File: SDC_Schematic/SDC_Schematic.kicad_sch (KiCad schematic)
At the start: 23 parts, among them J1 Screw_Terminal_01x02, J2 Screw_Terminal_01x02, J3 Screw_Terminal_01x02, J4 Conn_01x04, J5 Conn_01x04, J6 Conn_01x06_Socket, J7 Conn_01x03_Pin, J8 Conn_01x04, SW1 SW_SPST, U1 ATmega8A-P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

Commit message: modified schematic
added SPI port, capacitors for the servo & uC and barrel jack for power input
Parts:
- removed J3: Screw_Terminal_01x02, Capacitor_THT:C_Disc_D3.0mm_W1.6mm_P2.50mm, symbol Connector:Screw_Terminal_01x02
- added C5: 100nF, Capacitor_THT:C_Disc_D5.0mm_W2.5mm_P2.50mm, symbol Device:C_Small
- added C6: 100uF, symbol Device:C_Polarized
- added C7: 220uF, symbol Device:C_Polarized
- added J10: Jack-DC, symbol Connector:Jack-DC
- added J9: Conn_01x06_Socket, Connector_PinSocket_2.54mm:PinSocket_1x06_P2.54mm_Horizontal, symbol Connector:Conn_01x06_Socket
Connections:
- net +5V: now also C5.2, C6.1, C7.1, J9.6 (Pin_6)
- net GND: now also C5.1, C6.2, C7.2, J9.1 (Pin_1)
- net at U4.1 (IN+): now also J10.1
- net at U4.2 (IN-): now also J10.2
- net RST: now reaches C3.2, R1.2, SW1.2 (B), U1.1 (PC6/~{RESET})
- net RST: now also J9.5 (Pin_5)
- net MISO: now reaches U1.18 (PB4)
- net MISO: now also J9.3 (Pin_3)
- net SCK: now reaches U1.19 (PB5)
- net SCK: now also J9.4 (Pin_4)
- net SERVO renamed SERVO/MOSI
- net SERVO/MOSI: now also J9.2 (Pin_2)
- no-connect marks 8 -> 6
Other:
- note added: "SPI-For-Programming"
- moved on the sheet: J4, J5, J6, J7, J8, R2, R3, R4, R5, R6

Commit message: added part list
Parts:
- C6, C7: footprint (none) -> Capacitor_THT:CP_Radial_D6.3mm_P2.50mm
- J10: footprint (none) -> Connector_BarrelJack:BarrelJack_Horizontal
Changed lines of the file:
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@@
       (effects (font (size 1.27 1.27)) (justify left))
     )
-    (property "Footprint" "" (at 206.7052 45.72 0)
+    (property "Footprint" "Capacitor_THT:CP_Radial_D6.3mm_P2.50mm" (at 206.7052 45.72 0)
       (effects (font (size 1.27 1.27)) hide)
     )
@@
       (effects (font (size 1.27 1.27)))
     )
-    (property "Footprint" "" (at 40.64 45.466 0)
+    (property "Footprint" "Connector_BarrelJack:BarrelJack_Horizontal" (at 40.64 45.466 0)
       (effects (font (size 1.27 1.27)) hide)
     )
@@
       (effects (font (size 1.27 1.27)) (justify left))
     )
-    (property "Footprint" "" (at 157.1752 64.77 0)
-      (effects (font (size 1.27 1.27)) hide)
-    )
+    (property "Footprint" "Capacitor_THT:CP_Radial_D6.3mm_P2.50mm" (at 157.1752 64.77 0)
+      (effects (font (size 1.27 1.27)) hide)
+    )

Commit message: added mounting hole
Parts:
- added H1, H2, H3, H4: MountingHole, MountingHole:MountingHole_3.5mm, symbol Mechanical:MountingHole
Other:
- note added: "ANODE"
- note added: "CATHODE"
- note added: "EMITTER"
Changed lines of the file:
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@@
+    (stroke (width 0) (type default))
+  )
+  (polyline (pts (xy 125.73 179.07) (xy 125.73 160.02))
     (stroke (width 0) (type default))
   )
@@
     (stroke (width 0) (type default))
   )
+  (polyline (pts (xy 82.55 160.02) (xy 125.73 160.02))
+    (stroke (width 0) (type default))
+  )
   (polyline (pts (xy 29.21 58.42) (xy 95.25 58.42))
     (stroke (width 0) (type default))
@@
     (stroke (width 0) (type default))
   )
+  (polyline (pts (xy 82.55 179.07) (xy 125.73 179.07))
+    (stroke (width 0) (type default))
+  )
   (wire (pts (xy 139.7 147.32) (xy 140.97 147.32))
     (stroke (width 0) (type default))
@@
   )
   (wire (pts (xy 208.28 88.9) (xy 189.23 88.9))
+    (stroke (width 0) (type default))
+  )
+  (polyline (pts (xy 82.55 160.02) (xy 82.55 179.07))
     (stroke (width 0) (type default))
   )
@@
     (effects (font (size 1.5 1.5)) (justify left bottom))
   )
+  (text "EMITTER" (at 50.8 121.92 0)
+    (effects (font (size 1.27 1.27)) (justify left bottom))
+  )
+  (text "ANODE" (at 52.07 116.84 0)
+    (effects (font (size 1.27 1.27)) (justify left bottom))
+  )
   (text "SERVO" (at 199.39 29.21 0)
     (effects (font (size 3 3) (thickness 0.4) bold) (justify left bottom))
   )
+  (text "EMITTER" (at 50.8 144.78 0)
+    (effects (font (size 1.27 1.27)) (justify left bottom))
+  )
+  (text "CATHODE" (at 50.8 119.38 0)
+    (effects (font (size 1.27 1.27)) (justify left bottom))
+  )
+  (text "ANODE" (at 52.07 139.7 0)
+    (effects (font (size 1.27 1.27)) (justify left bottom))
+  )
   (text "POWER SUPPLY" (at 29.21 29.21 0)
     (effects (font (size 3 3) (thickness 0.6) bold) (justify left bottom))
@@
     (effects (font (size 3 3) bold) (justify left bottom))
   )
+  (text "CATHODE" (at 50.8 142.24 0)
+    (effects (font (size 1.27 1.27)) (justify left bottom))
+  )
   (label "RST" (at 48.26 170.18 180) (fields_autoplaced)
     (effects (font (size 1.27 1.27)) (justify right bottom))
@@
     (effects (font (size 1.27 1.27) bold) (justify left bottom))
   )
-  (label "EMITTER" (at 50.8 144.78 0) (fields_autoplaced)
-    (effects (font (size 1.27 1.27)) (justify left bottom))
-  )
   (label "SERVO{slash}MOSI" (at 167.64 88.9 180) (fields_autoplaced)
     (effects (font (size 1.27 1.27)) (justify right bottom))
   )
   (label "EN3,4" (at 201.93 109.22 0) (fields_autoplaced)
-    (effects (font (size 1.27 1.27)) (justify left bottom))
-  )
-  (label "CATHODE" (at 50.8 142.24 0) (fields_autoplaced)
     (effects (font (size 1.27 1.27)) (justify left bottom))
   )
@@
     (effects (font (size 1.27 1.27) bold) (justify left bottom))
   )
-  (label "ANODE" (at 58.42 116.84 180) (fields_autoplaced)
-    (effects (font (size 1.27 1.27)) (justify right bottom))
-  )
   (label "RX0" (at 203.2 154.94 0) (fields_autoplaced)
     (effects (font (size 1.27 1.27)) (justify left bottom))
@@
     (effects (font (size 1.27 1.27)) (justify right bottom))
   )
-  (label "CATHODE" (at 50.8 119.38 0) (fields_autoplaced)
-    (effects (font (size 1.27 1.27)) (justify left bottom))
-  )
-  (label "ANODE" (at 52.07 139.7 0) (fields_autoplaced)
-    (effects (font (size 1.27 1.27)) (justify left bottom))
-  )
   (label "EN1,2" (at 201.93 93.98 0) (fields_autoplaced)
     (effects (font (size 1.27 1.27)) (justify left bottom))
@@
   (label "EN1,2" (at 163.83 83.82 180) (fields_autoplaced)
     (effects (font (size 1.27 1.27)) (justify right bottom))
-  )
-  (label "EMITTER" (at 50.8 121.92 0) (fields_autoplaced)
-    (effects (font (size 1.27 1.27)) (justify left bottom))
   )
   (symbol (lib_id "Connector:Conn_01x06_Socket") (at 36.83 175.26 180) (unit 1)
@@
     )
   )
+  (symbol (lib_id "Mechanical:MountingHole") (at 107.95 163.83 0) (unit 1)
+    (in_bom yes) (on_board yes) (dnp no) (fields_autoplaced)
+    (property "Reference" "H2" (at 110.49 162.56 0)
+      (effects (font (size 1.27 1.27)) (justify left))
+    )
+    (property "Value" "MountingHole" (at 110.49 165.1 0)
+      (effects (font (size 1.27 1.27)) (justify left))
+    )
+    (property "Footprint" "MountingHole:MountingHole_3.5mm" (at 107.95 163.83 0)
+      (effects (font (size 1.27 1.27)) hide)
+    )
+    (property "Datasheet" "~" (at 107.95 163.83 0)
+      (effects (font (size 1.27 1.27)) hide)
+    )
+    (instances
+      (project "SDC_Schematic"
+        (path "/f4146ac7-8f5d-4d47-a7f7-55c436dc7aff"
+          (reference "H2") (unit 1)
+        )
+      )
+    )
+  )
   (symbol (lib_id "Device:R") (at 52.07 147.32 90) (unit 1)
     (in_bom yes) (on_board yes) (dnp no)
@@
     )
   )
+  (symbol (lib_id "Mechanical:MountingHole") (at 107.95 173.99 0) (unit 1)
+    (in_bom yes) (on_board yes) (dnp no) (fields_autoplaced)
+    (property "Reference" "H4" (at 110.49 172.72 0)
+      (effects (font (size 1.27 1.27)) (justify left))
+    )
+    (property "Value" "MountingHole" (at 110.49 175.26 0)
+      (effects (font (size 1.27 1.27)) (justify left))
+    )
+    (property "Footprint" "MountingHole:MountingHole_3.5mm" (at 107.95 173.99 0)
+      (effects (font (size 1.27 1.27)) hide)
+    )
+    (property "Datasheet" "~" (at 107.95 173.99 0)
+      (effects (font (size 1.27 1.27)) hide)
+    )
+    (instances
+      (project "SDC_Schematic"
+        (path "/f4146ac7-8f5d-4d47-a7f7-55c436dc7aff"
+          (reference "H4") (unit 1)
+        )
+      )
+    )
+  )
   (symbol (lib_id "power:GND") (at 140.97 148.59 0) (unit 1)
     (in_bom yes) (on_board yes) (dnp no) (fields_autoplaced)
@@
         (path "/f4146ac7-8f5d-4d47-a7f7-55c436dc7aff"
           (reference "#PWR04") (unit 1)
+        )
+      )
+    )
+  )
+  (symbol (lib_id "Mechanical:MountingHole") (at 86.36 173.99 0) (unit 1)
+    (in_bom yes) (on_board yes) (dnp no) (fields_autoplaced)
+    (property "Reference" "H3" (at 88.9 172.72 0)
+      (effects (font (size 1.27 1.27)) (justify left))
+    )
+    (property "Value" "MountingHole" (at 88.9 175.26 0)
+      (effects (font (size 1.27 1.27)) (justify left))
+    )
+    (property "Footprint" "MountingHole:MountingHole_3.5mm" (at 86.36 173.99 0)
+      (effects (font (size 1.27 1.27)) hide)
+    )
+    (property "Datasheet" "~" (at 86.36 173.99 0)
+      (effects (font (size 1.27 1.27)) hide)
+    )
+    (instances
+      (project "SDC_Schematic"
+        (path "/f4146ac7-8f5d-4d47-a7f7-55c436dc7aff"
+          (reference "H3") (unit 1)
         )
       )
@@
         )
       )
+    )
+  )
+  (symbol (lib_id "Mechanical:MountingHole") (at 86.36 163.83 0) (unit 1)
+    (in_bom yes) (on_board yes) (dnp no) (fields_autoplaced)
+    (property "Reference" "H1" (at 88.9 162.56 0)
+      (effects (font (size 1.27 1.27)) (justify left))
+    )
+    (property "Value" "MountingHole" (at 88.9 165.1 0)
+      (effects (font (size 1.27 1.27)) (justify left))
+    )
+    (property "Footprint" "MountingHole:MountingHole_3.5mm" (at 86.36 163.83 0)
+      (effects (font (size 1.27 1.27)) hide)
+    )
+    (property "Datasheet" "~" (at 86.36 163.83 0)
+      (effects (font (size 1.27 1.27)) hide)
+    )
+    (instances
+      (project "SDC_Schematic"
+        (path "/f4146ac7-8f5d-4d47-a7f7-55c436dc7aff"
+          (reference "H1") (unit 1)
+        )
+      )

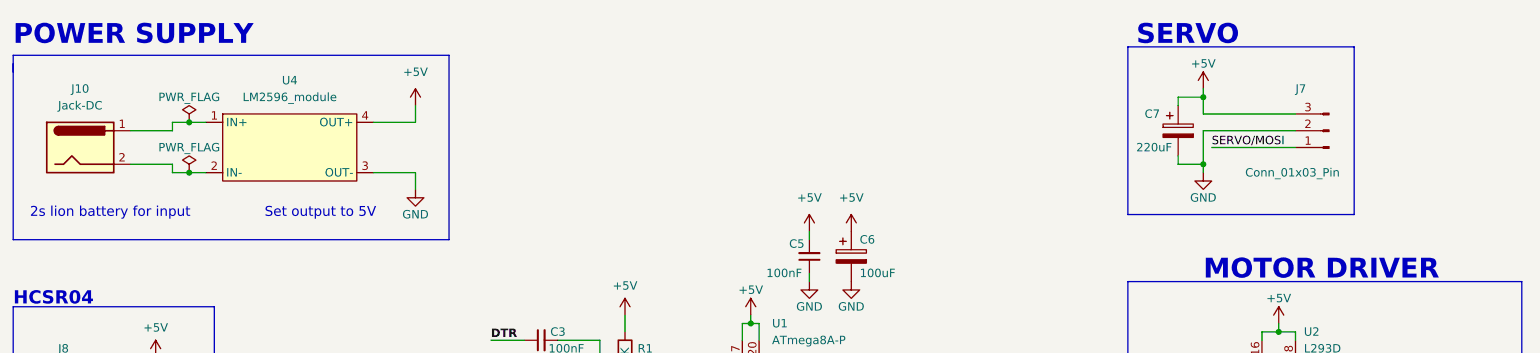
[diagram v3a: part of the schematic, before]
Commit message: Schematic and PCB
updated schematic symbols and connections as well as created a PCB along with gerber files
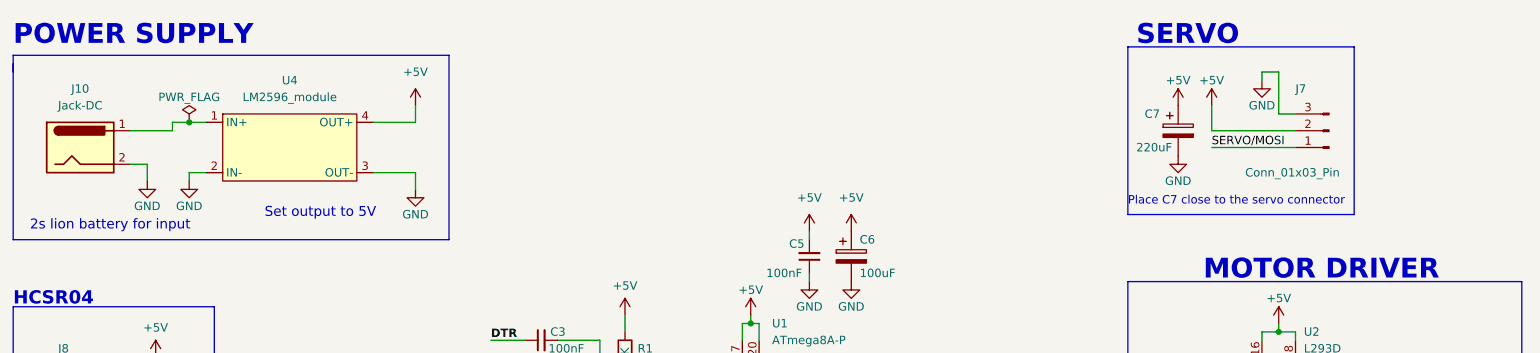
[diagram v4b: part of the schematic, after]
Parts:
- J6, J9: footprint Connector_PinSocket_2.54mm:PinSocket_1x06_P2.54mm_Horizontal -> Connector_PinSocket_2.54mm:PinSocket_1x06_P2.54mm_Vertical
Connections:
- net +5V: now also J7.2 (Pin_2); no longer J7.3 (Pin_3)
- net GND: now also J10.2, J7.3 (Pin_3), U4.2 (IN-); no longer J7.2 (Pin_2)
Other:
- note added: "Place C7 close to the servo connector"
